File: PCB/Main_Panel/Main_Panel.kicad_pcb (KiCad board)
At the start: 2 copper layers, 170 x 170 mm, 0 parts

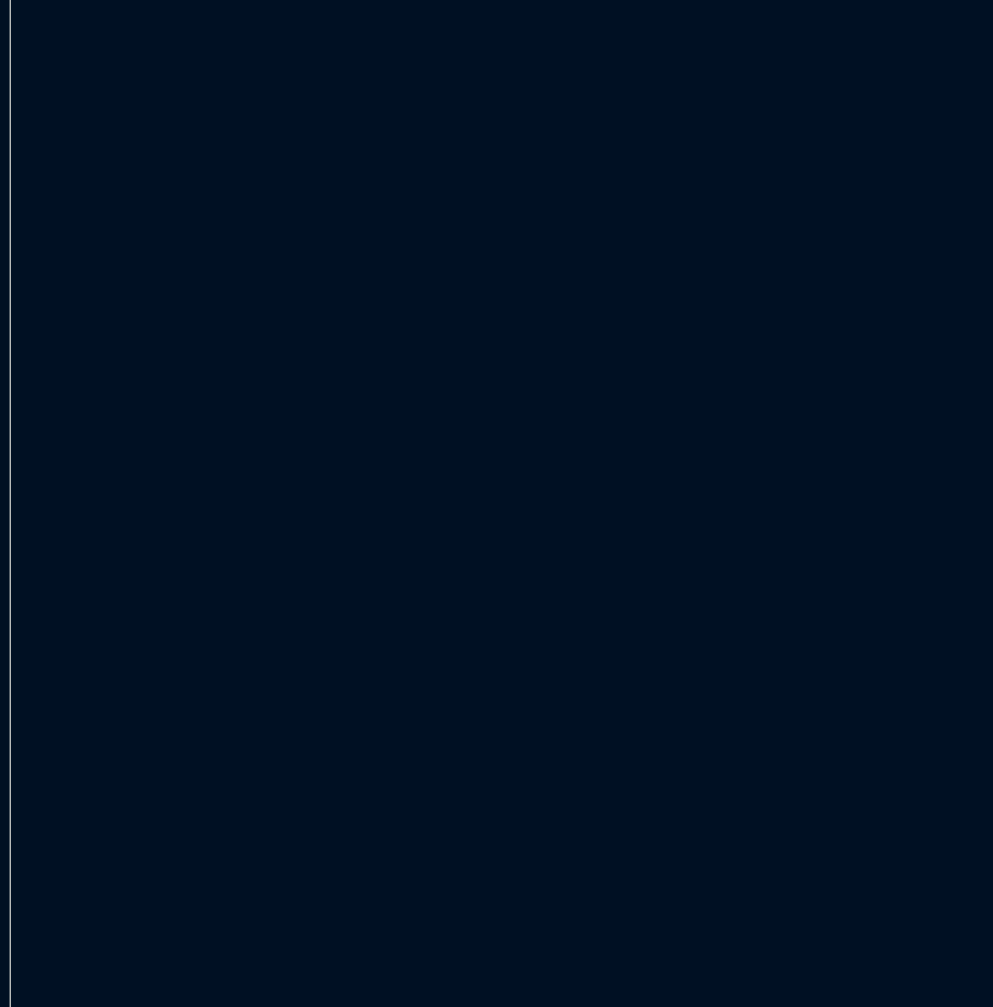
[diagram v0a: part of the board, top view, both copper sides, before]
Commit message: Fill kicad libraries
Finished the kicad symbol and footprint libraries and linked them together so everything works as intended.
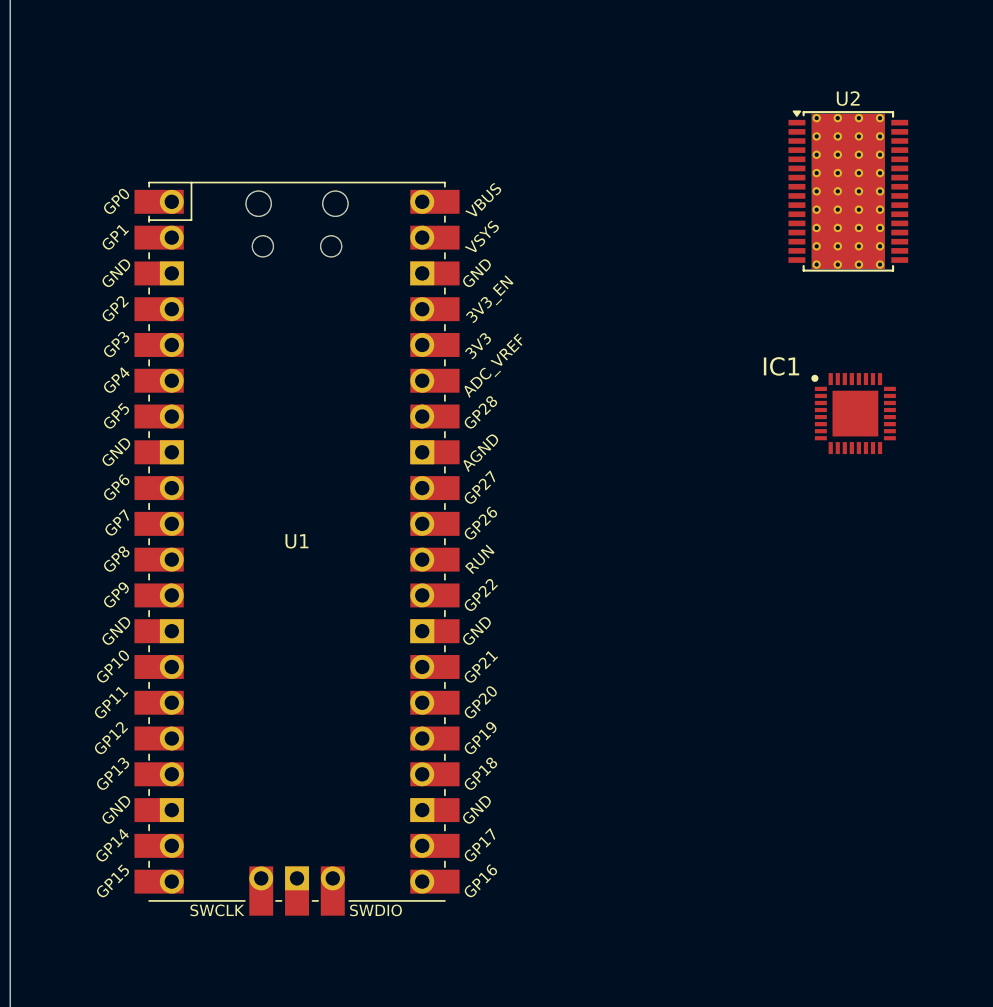
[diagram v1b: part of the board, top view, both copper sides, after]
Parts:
- added IC1: TCA6424ARGJR, Control_Panel_Footprints:QFN50P500X500X60-33N-D, F.Cu at (84.0, 81.0)
- added U1: Pico, Control_Panel_Footprints:RPi_Pico_SMD_TH, F.Cu at (44.4, 90.1)
- added U2: TLC5947DAP, Package_SO:HTSSOP-32-1EP_6.1x11mm_P0.65mm_EP5.2x11mm_Mask4.11x4.36mm_ThermalVias, F.Cu at (83.5, 65.2)

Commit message: PCB Designs
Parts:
- added C1: 0.01uF, Capacitor_SMD:C_0805_2012Metric, B.Cu at (167.3, 163.8)
- added C2: 0.01uF, Capacitor_SMD:C_0805_2012Metric, B.Cu at (162.6, 163.8)
- added C3: 0.01uF, Capacitor_SMD:C_0805_2012Metric, B.Cu at (187.4, 163.2)
- added C4: 0.01uF, Capacitor_SMD:C_0805_2012Metric, B.Cu at (182.2, 163.2)
- added H1: MountingHole_Pad, MountingHole:MountingHole_3.2mm_M3_DIN965_Pad, F.Cu at (65.0, 65.0)
- added H10: MountingHole_Pad, MountingHole:MountingHole_3.2mm_M3_DIN965_Pad, F.Cu at (220.5, 117.5)
- added H11: MountingHole_Pad, MountingHole:MountingHole_3.2mm_M3_DIN965_Pad, F.Cu at (64.5, 167.5)
- added H12: MountingHole_Pad, MountingHole:MountingHole_3.2mm_M3_DIN965_Pad, F.Cu at (135.5, 167.5)
- added H13: MountingHole_Pad, MountingHole:MountingHole_3.2mm_M3_DIN965_Pad, F.Cu at (64.5, 220.5)
- added H14: MountingHole_Pad, MountingHole:MountingHole_3.2mm_M3_DIN965_Pad, F.Cu at (135.5, 220.5)
- added H15: MountingHole_Pad, MountingHole:MountingHole_3.2mm_M3_DIN965_Pad, F.Cu at (148.0, 165.0)
- added H16: MountingHole_Pad, MountingHole:MountingHole_3.2mm_M3_DIN965_Pad, F.Cu at (220.0, 165.0)
- added H17: MountingHole_Pad, MountingHole:MountingHole_3.2mm_M3_DIN965_Pad, F.Cu at (220.0, 187.0)
- added H18: MountingHole_Pad, MountingHole:MountingHole_3.2mm_M3_DIN965_Pad, F.Cu at (148.0, 187.0)
- added H19: MountingHole_Pad, MountingHole:MountingHole_3.2mm_M3_DIN965_Pad, F.Cu at (170.0, 200.0)
- added H2: MountingHole_Pad, MountingHole:MountingHole_3.2mm_M3_DIN965_Pad, F.Cu at (132.0, 65.0)
- added H20: MountingHole_Pad, MountingHole:MountingHole_3.2mm_M3_DIN965_Pad, F.Cu at (170.0, 217.0)
- added H21: MountingHole_Pad, MountingHole:MountingHole_3.2mm_M3_DIN965_Pad, F.Cu at (198.0, 200.0)
- added H22: MountingHole_Pad, MountingHole:MountingHole_3.2mm_M3_DIN965_Pad, F.Cu at (198.0, 217.0)
- added H3: MountingHole_Pad, MountingHole:MountingHole_3.2mm_M3_DIN965_Pad, F.Cu at (132.0, 122.0)
- added H4: MountingHole_Pad, MountingHole:MountingHole_3.2mm_M3_DIN965_Pad, F.Cu at (198.5, 130.0)
- added H5: MountingHole_Pad, MountingHole:MountingHole_3.2mm_M3_DIN965_Pad, F.Cu at (198.5, 152.0)
- added H6: MountingHole_Pad, MountingHole:MountingHole_3.2mm_M3_DIN965_Pad, F.Cu at (86.5, 152.0)
- added H7: MountingHole_Pad, MountingHole:MountingHole_3.2mm_M3_DIN965_Pad, F.Cu at (149.5, 64.5)
- added H8: MountingHole_Pad, MountingHole:MountingHole_3.2mm_M3_DIN965_Pad, F.Cu at (220.5, 64.5)
- added H9: MountingHole_Pad, MountingHole:MountingHole_3.2mm_M3_DIN965_Pad, F.Cu at (149.5, 117.5)
- added HS1: Heatsink_Pad, Control_Panel_Footprints:Heat Sink, F.Cu at (87.7, 42.5)
- added J1: Conn_02x11_Odd_Even, Connector_PinHeader_2.54mm:PinHeader_2x11_P2.54mm_Vertical, F.Cu at (183.1, 85.5)
- added J2: Conn_02x11_Odd_Even, Connector_PinHeader_2.54mm:PinHeader_2x11_P2.54mm_Vertical, F.Cu at (98.1, 188.5)
- added J3: Conn_01x05, Connector_PinHeader_2.54mm:PinHeader_1x05_P2.54mm_Vertical, F.Cu at (184.0, 170.0)
- added J4: Conn_01x05, Connector_PinHeader_2.54mm:PinHeader_1x05_P2.54mm_Vertical, F.Cu at (189.0, 199.0)
- added J5: Conn_01x15, Connector_PinHeader_2.54mm:PinHeader_1x15_P2.54mm_Vertical, F.Cu at (81.0, 116.0)
- added R1: 10k, Resistor_SMD:R_0805_2012Metric, B.Cu at (106.0, 140.1)
- added R2: 10k, Resistor_SMD:R_0805_2012Metric, B.Cu at (123.6, 79.2)
- added R3: 10k, Resistor_SMD:R_0805_2012Metric, B.Cu at (122.8, 74.5)
- added R30: 10k, Resistor_SMD:R_0805_2012Metric, B.Cu at (159.5, 160.1)
- added R31: 10k, Resistor_SMD:R_0805_2012Metric, B.Cu at (171.5, 163.8)
- added R32: 10k, Resistor_SMD:R_0805_2012Metric, B.Cu at (173.0, 159.1)
- added R33: 10k, Resistor_SMD:R_0805_2012Metric, B.Cu at (158.7, 164.0)
- added R34: 10k, Resistor_SMD:R_0805_2012Metric, B.Cu at (193.2, 159.0)
- added R35: 10k, Resistor_SMD:R_0805_2012Metric, B.Cu at (176.8, 159.1)
- added R36: 10k, Resistor_SMD:R_0805_2012Metric, B.Cu at (192.7, 163.8)
- added R37: 10k, Resistor_SMD:R_0805_2012Metric, B.Cu at (177.6, 163.5)
- added R4: 10k, Resistor_SMD:R_0805_2012Metric, B.Cu at (101.2, 140.2)
- added R5: 2460, Resistor_SMD:R_0805_2012Metric, B.Cu at (126.8, 152.8)
- IC1, U1, U2: moved to B.Cu
- moved U2 96.5 mm to (145.5, 139.2), turned to -90 degrees
- moved U1 59.9 mm to (104.1, 86.0), turned to 180 degrees
- moved IC1 58.5 mm to (110.2, 133.3)
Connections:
- IC1 pad 1: unconnected-(IC1-P00-Pad1) -> /Switch2
- IC1 pad 10: unconnected-(IC1-P11-Pad10) -> /Switch11
- IC1 pad 11: unconnected-(IC1-P12-Pad11) -> /Switch12
- IC1 pad 12: unconnected-(IC1-P13-Pad12) -> /Switch13
- IC1 pad 13: unconnected-(IC1-P14-Pad13) -> /Button0
- IC1 pad 14: unconnected-(IC1-P15-Pad14) -> /Button1
- IC1 pad 15: unconnected-(IC1-P16-Pad15) -> /Button2
- IC1 pad 16: unconnected-(IC1-P17-Pad16) -> /Button3
- IC1 pad 17: unconnected-(IC1-P20-Pad17) -> /Button4
- IC1 pad 18: unconnected-(IC1-P21-Pad18) -> /Button5
- IC1 pad 19: unconnected-(IC1-P22-Pad19) -> /Button6
- IC1 pad 2: unconnected-(IC1-P01-Pad2) -> /Switch3
- IC1 pad 20: unconnected-(IC1-P23-Pad20) -> /Button7
- IC1 pad 21: unconnected-(IC1-P24-Pad21) -> /Button8
- IC1 pad 22: unconnected-(IC1-P25-Pad22) -> /Button9
- IC1 pad 23: unconnected-(IC1-P26-Pad23) -> /Button10
- IC1 pad 24: unconnected-(IC1-P27-Pad24) -> /Button11
- IC1 pad 25: unconnected-(IC1-GND-Pad25) -> GND
- IC1 pad 26: unconnected-(IC1-ADDR-Pad26) -> GND
- IC1 pad 27: unconnected-(IC1-V_CCP-Pad27) -> +3.3V
- IC1 pad 28: unconnected-(IC1-~{RESET}-Pad28) -> Net-(IC1-~{RESET})
- IC1 pad 29: unconnected-(IC1-SCL-Pad29) -> SCL
- IC1 pad 3: unconnected-(IC1-P02-Pad3) -> /Switch4
- IC1 pad 30: unconnected-(IC1-SDA-Pad30) -> SDA
- IC1 pad 31: unconnected-(IC1-V_CCI-Pad31) -> +3.3V
- IC1 pad 32: unconnected-(IC1-~{INT}-Pad32) -> Net-(IC1-~{INT})
- IC1 pad 4: unconnected-(IC1-P03-Pad4) -> /Switch5
- IC1 pad 5: unconnected-(IC1-P04-Pad5) -> /Switch6
- IC1 pad 6: unconnected-(IC1-P05-Pad6) -> /Switch7
- IC1 pad 7: unconnected-(IC1-P06-Pad7) -> /Switch8
- IC1 pad 8: unconnected-(IC1-P07-Pad8) -> /Switch9
- IC1 pad 9: unconnected-(IC1-P10-Pad9) -> /Switch10
- U1 pad 1: unconnected-(U1-GPIO0-Pad1) -> /Encoder_0_B
- U1 pad 10: unconnected-(U1-GPIO7-Pad10) -> /Switch1
- U1 pad 13: unconnected-(U1-GND-Pad13) -> GND
- U1 pad 18: unconnected-(U1-GND-Pad18) -> GND
- U1 pad 2: unconnected-(U1-GPIO1-Pad2) -> /Encoder_0_A
- U1 pad 21: unconnected-(U1-GPIO16-Pad21) -> XLAT
- U1 pad 22: unconnected-(U1-GPIO17-Pad22) -> Blank
- U1 pad 23: unconnected-(U1-GND-Pad23) -> GND
- U1 pad 24: unconnected-(U1-GPIO18-Pad24) -> SCK
- U1 pad 25: unconnected-(U1-GPIO19-Pad25) -> MOSI
- U1 pad 28: unconnected-(U1-GND-Pad28) -> GND
- U1 pad 3: unconnected-(U1-GND-Pad3) -> GND
- U1 pad 31: unconnected-(U1-GPIO26_ADC0-Pad31) -> /Pot2
- U1 pad 32: unconnected-(U1-GPIO27_ADC1-Pad32) -> /Pot1
- U1 pad 33: unconnected-(U1-AGND-Pad33) -> GND
- U1 pad 34: unconnected-(U1-GPIO28_ADC2-Pad34) -> /Pot0
- U1 pad 36: unconnected-(U1-3V3-Pad36) -> +3.3V
- U1 pad 38: unconnected-(U1-GND-Pad38) -> GND
- U1 pad 39: unconnected-(U1-VSYS-Pad39) -> +5V
- U1 pad 4: unconnected-(U1-GPIO2-Pad4) -> /Encoder_1_B
- U1 pad 40: unconnected-(U1-VBUS-Pad40) -> +5V
- U1 pad 5: unconnected-(U1-GPIO3-Pad5) -> /Encoder_1_A
- U1 pad 6: unconnected-(U1-GPIO4-Pad6) -> SDA
- U1 pad 7: unconnected-(U1-GPIO5-Pad7) -> SCL
- U1 pad 8: unconnected-(U1-GND-Pad8) -> GND
- U1 pad 9: unconnected-(U1-GPIO6-Pad9) -> /Switch0
- U2 pad 1: unconnected-(U2-GND-Pad1) -> GND
- U2 pad 10: unconnected-(U2-OUT5-Pad10) -> /LED9
- U2 pad 11: unconnected-(U2-OUT6-Pad11) -> /LED8
- U2 pad 12: unconnected-(U2-OUT7-Pad12) -> /LED7
- U2 pad 13: unconnected-(U2-OUT8-Pad13) -> /LED6
- U2 pad 14: unconnected-(U2-OUT9-Pad14) -> /LED5
- U2 pad 15: unconnected-(U2-OUT10-Pad15) -> /LED4
- U2 pad 16: unconnected-(U2-OUT11-Pad16) -> /LED3
- U2 pad 17: unconnected-(U2-OUT12-Pad17) -> /LED12
- U2 pad 18: unconnected-(U2-OUT13-Pad18) -> /LED13
- U2 pad 19: unconnected-(U2-OUT14-Pad19) -> /LED14
- U2 pad 2: unconnected-(U2-BLANK-Pad2) -> Blank
- U2 pad 20: unconnected-(U2-OUT15-Pad20) -> /LED23
- U2 pad 21: unconnected-(U2-OUT16-Pad21) -> /LED22
- U2 pad 22: unconnected-(U2-OUT17-Pad22) -> /LED21
- U2 pad 23: unconnected-(U2-OUT18-Pad23) -> /LED20
- U2 pad 24: unconnected-(U2-OUT19-Pad24) -> /LED19
- U2 pad 25: unconnected-(U2-OUT20-Pad25) -> /LED18
- U2 pad 26: unconnected-(U2-OUT21-Pad26) -> /LED17
- U2 pad 27: unconnected-(U2-OUT22-Pad27) -> /LED16
- U2 pad 28: unconnected-(U2-OUT23-Pad28) -> /LED15
- U2 pad 3: unconnected-(U2-SCLK-Pad3) -> SCK
- U2 pad 30: unconnected-(U2-XLAT-Pad30) -> XLAT
- U2 pad 31: unconnected-(U2-IREF-Pad31) -> Net-(U2-IREF)
- U2 pad 32: unconnected-(U2-VCC-Pad32) -> +3.3V
- U2 pad 33: unconnected-(U2-PowerPAD-Pad33) -> Net-(U2-PowerPAD)
- U2 pad 4: unconnected-(U2-SIN-Pad4) -> MOSI
- U2 pad 5: unconnected-(U2-OUT0-Pad5) -> /LED0
- U2 pad 6: unconnected-(U2-OUT1-Pad6) -> /LED1
- U2 pad 7: unconnected-(U2-OUT2-Pad7) -> /LED2
- U2 pad 8: unconnected-(U2-OUT3-Pad8) -> /LED11
- U2 pad 9: unconnected-(U2-OUT4-Pad9) -> /LED10
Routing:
- net GND: track 0.00 -> 1168.7 mm, vias 0 -> 1
- net +3.3V: track 0.00 -> 502.5 mm, vias 0 -> 1
- net +5V: track 0.00 -> 328.0 mm
- net /Pot0: track 0.00 -> 166.1 mm
- net /Pot1: track 0.00 -> 160.6 mm
- net /Pot2: track 0.00 -> 156.9 mm
- net /LED3: track 0.00 -> 151.0 mm
- net /LED4: track 0.00 -> 144.8 mm
- net /LED5: track 0.00 -> 138.4 mm
- net /Encoder_0_B: track 0.00 -> 136.2 mm, vias 0 -> 1
- net /LED6: track 0.00 -> 132.3 mm
- net /Encoder_0_A: track 0.00 -> 129.6 mm, vias 0 -> 1
- net /LED7: track 0.00 -> 126.3 mm
- net /LED8: track 0.00 -> 120.0 mm
- net /Encoder_1_B: track 0.00 -> 119.5 mm, vias 0 -> 1
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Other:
- board size 170 x 170 mm -> 165 x 165 mm

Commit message: PCB Manufacturing Files and Full CAD
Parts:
- moved HS1 115.5 mm to (139.2, 145.9)
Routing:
- net +5V: track 328.0 -> 429.1 mm
- net GND: track 1168.7 -> 1199.6 mm, vias 1 -> 0
- net SDA: track 105.3 -> 104.2 mm
- net /Switch9: track 16.5 -> 15.8 mm
- net Blank: track 59.7 -> 59.0 mm
- net /Button6: track 74.1 -> 73.5 mm
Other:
- board text added: "Button Panel 1"
- board text added: "Button Panel 2"
- board text added: "Flight Sim USB Control Panel v1.0 Tolga Cavusoglu September 2025"
- board text added: "Potentiometers"
- board text added: "RP Pico 2"
- board text added: "R_IREF"
- board text added: "Rotary Encoders"
- board text added: "Switch Panel"
- board text added: "TCA6424ARGJR I2C Port Expander"
- board text added: "TLC5947 LED Driver"

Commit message: Update main and button pcbs to fix errors with v1.0
Added pull downs to gpio expander and changed header footprint
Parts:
- added R10: 10k, Resistor_SMD:R_0805_2012Metric, B.Cu at (162.8, 89.9)
- added R11: 10k, Resistor_SMD:R_0805_2012Metric, B.Cu at (88.4, 142.2)
- added R12: 10k, Resistor_SMD:R_0805_2012Metric, B.Cu at (85.6, 144.8)
- added R13: 10k, Resistor_SMD:R_0805_2012Metric, B.Cu at (75.8, 124.5)
- added R14: 10k, Resistor_SMD:R_0805_2012Metric, B.Cu at (94.8, 153.5)
- added R15: 10k, Resistor_SMD:R_0805_2012Metric, B.Cu at (98.1, 149.8)
- added R16: 10k, Resistor_SMD:R_0805_2012Metric, B.Cu at (90.1, 158.5)
- added R17: 10k, Resistor_SMD:R_0805_2012Metric, B.Cu at (86.3, 162.0)
- added R18: 10k, Resistor_SMD:R_0805_2012Metric, B.Cu at (81.9, 165.8)
- added R19: 10k, Resistor_SMD:R_0805_2012Metric, B.Cu at (160.5, 86.0)
- added R20: 10k, Resistor_SMD:R_0805_2012Metric, B.Cu at (77.6, 169.5)
- added R21: 10k, Resistor_SMD:R_0805_2012Metric, B.Cu at (157.8, 89.9)
- added R22: 10k, Resistor_SMD:R_0805_2012Metric, B.Cu at (75.8, 129.8)
- added R23: 10k, Resistor_SMD:R_0805_2012Metric, B.Cu at (79.3, 132.5)
- added R24: 10k, Resistor_SMD:R_0805_2012Metric, B.Cu at (75.8, 134.8)
- added R25: 10k, Resistor_SMD:R_0805_2012Metric, B.Cu at (79.6, 137.0)
- added R26: 10k, Resistor_SMD:R_0805_2012Metric, B.Cu at (88.1, 133.0)
- added R27: 10k, Resistor_SMD:R_0805_2012Metric, B.Cu at (84.9, 135.2)
- added R28: 10k, Resistor_SMD:R_0805_2012Metric, B.Cu at (88.6, 137.8)
- added R29: 10k, Resistor_SMD:R_0805_2012Metric, B.Cu at (84.9, 140.0)
- added R6: 10k, Resistor_SMD:R_0805_2012Metric, B.Cu at (150.2, 86.2)
- added R7: 10k, Resistor_SMD:R_0805_2012Metric, B.Cu at (152.8, 89.9)
- added R8: 10k, Resistor_SMD:R_0805_2012Metric, B.Cu at (79.3, 127.0)
- added R9: 10k, Resistor_SMD:R_0805_2012Metric, B.Cu at (155.5, 85.9)
- moved J2 11.6 mm to (86.8, 191.0)
- moved J1 11.6 mm to (171.8, 88.0)
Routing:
- net GND: track 1199.6 -> 1373.8 mm
- net /Switch13: track 17.6 -> 55.4 mm, vias 0 -> 4
- net /Switch11: track 16.4 -> 49.5 mm, vias 0 -> 4
- net /Switch10: track 15.5 -> 48.3 mm, vias 0 -> 4
- net /Button6: track 73.5 -> 104.9 mm, vias 0 -> 2
- net /Switch12: track 16.7 -> 47.0 mm, vias 0 -> 4
- net /Button7: track 79.7 -> 106.9 mm, vias 0 -> 2
- net /Switch8: track 18.1 -> 43.5 mm, vias 0 -> 4
- net /Switch9: track 15.8 -> 41.1 mm, vias 0 -> 4
- net /Button8: track 83.5 -> 108.0 mm, vias 0 -> 2
- net /Switch5: track 24.8 -> 48.2 mm, vias 0 -> 4
- net /Button9: track 88.2 -> 109.8 mm, vias 0 -> 2
- net /Switch4: track 27.3 -> 47.5 mm, vias 0 -> 4
- net /Button10: track 92.6 -> 111.8 mm, vias 0 -> 2
- net /Switch7: track 20.0 -> 37.6 mm, vias 0 -> 4
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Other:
- board text added: "Flight Sim USB Control Panel v1.1 Tolga Cavusoglu September 2025"
- board text removed: "Flight Sim USB Control Panel v1.0 Tolga Cavusoglu September 2025"

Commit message: Add manufacturing files for v1.1
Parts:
- added R38: 10k, Resistor_SMD:R_0805_2012Metric, B.Cu at (80.2, 106.0)
- added R39: 10k, Resistor_SMD:R_0805_2012Metric, B.Cu at (80.4, 101.0)
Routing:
- net /Switch1: track 46.7 -> 69.7 mm
- net GND: track 1373.8 -> 1387.6 mm
- net /Switch0: track 50.8 -> 62.6 mm
